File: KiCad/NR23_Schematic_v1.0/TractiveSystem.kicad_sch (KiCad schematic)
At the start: 3 parts

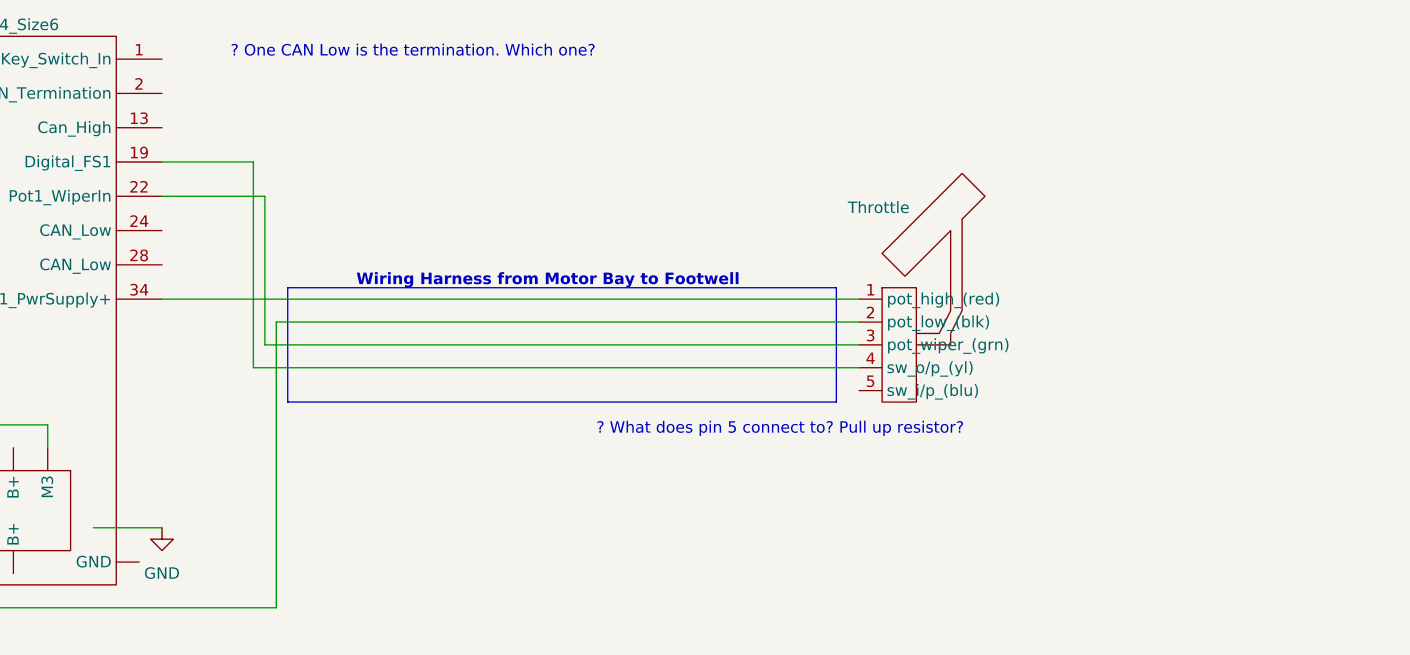
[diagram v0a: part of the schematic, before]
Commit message: added pullup resistor to the throttle
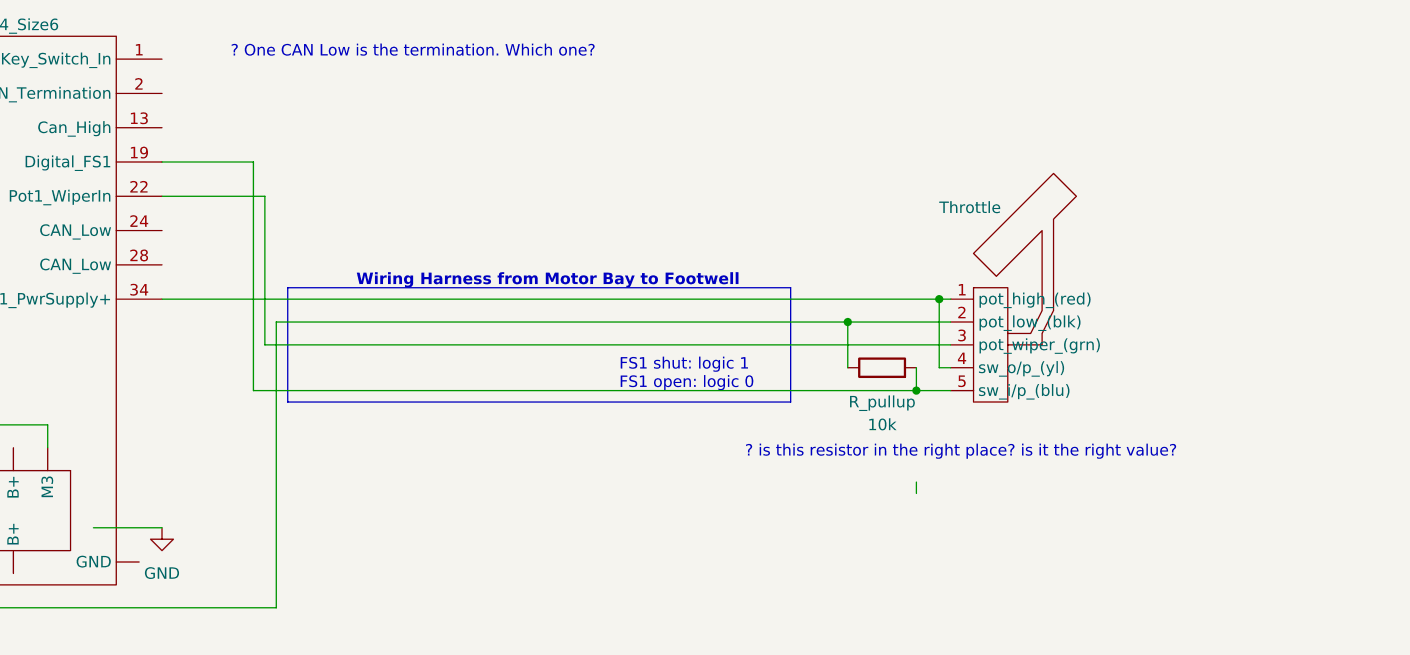
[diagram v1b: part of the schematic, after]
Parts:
- added R_pullup: 10k, symbol Device:R
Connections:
- net at U?.1 (pot_high_(red)), U?.34 (Pot1_PwrSupply+): now also U?.4 (sw_o/p_(yl))
- net at U?. (M3), U?.2 (pot_low_(blk)): now also R_pullup.1
- net at U?.19 (Digital_FS1): now also U?.5 (sw_i/p_(blu)), R_pullup.2; no longer U?.4 (sw_o/p_(yl))
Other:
- note added: "? is this resistor in the right place? is it the right value?"
- note added: "FS1 shut: logic 1 FS1 open: logic 0"
- note removed: "? What does pin 5 connect to? Pull up resistor?"
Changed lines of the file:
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@@
 (kicad_sch (version 20211123) (generator eeschema)
   (paper "A")
+  (junction (at 228.6 135.89) (diameter 0) (color 0 0 0 0)
+  )
+  (junction (at 231.14 125.73) (diameter 0) (color 0 0 0 0)
+  )
+  (junction (at 220.98 128.27) (diameter 0) (color 0 0 0 0)
+  )
   (bus_entry (at 88.9 180.34) (size 2.54 -2.54)
     (stroke (width 0) (type default) (color 0 0 0 0))
@@
     (stroke (width 0) (type default) (color 0 0 0 0))
   )
-  (polyline (pts (xy 219.71 124.46) (xy 158.75 124.46))
+  (polyline (pts (xy 214.63 124.46) (xy 158.75 124.46))
     (stroke (width 0) (type default) (color 0 0 0 0))
   )
@@
     (stroke (width 0) (type default) (color 0 0 0 0))
   )
+  (wire (pts (xy 154.94 110.49) (xy 154.94 135.89))
+    (stroke (width 0) (type default) (color 0 0 0 0))
+  )
   (polyline (pts (xy 106.68 135.89) (xy 45.72 135.89))
     (stroke (width 0) (type default) (color 0 0 0 0))
   )
+  (wire (pts (xy 154.94 135.89) (xy 228.6 135.89))
+    (stroke (width 0) (type default) (color 0 0 0 0))
+  )
   (polyline (pts (xy 55.88 170.18) (xy 55.88 146.05))
     (stroke (width 0) (type default) (color 0 0 0 0))
   )
+  (wire (pts (xy 220.98 128.27) (xy 232.41 128.27))
+    (stroke (width 0) (type default) (color 0 0 0 0))
+  )
   (wire (pts (xy 124.46 142.24) (xy 124.46 140.97))
     (stroke (width 0) (type default) (color 0 0 0 0))
   )
-  (wire (pts (xy 144.78 125.73) (xy 222.25 125.73))
+  (wire (pts (xy 144.78 125.73) (xy 231.14 125.73))
     (stroke (width 0) (type default) (color 0 0 0 0))
   )
@@
     (stroke (width 0) (type default) (color 0 0 0 0))
   )
+  (wire (pts (xy 228.6 135.89) (xy 232.41 135.89))
+    (stroke (width 0) (type default) (color 0 0 0 0))
+  )
+  (wire (pts (xy 220.98 128.27) (xy 220.98 133.35))
+    (stroke (width 0) (type default) (color 0 0 0 0))
+  )
   (wire (pts (xy 156.21 130.81) (xy 156.21 114.3))
     (stroke (width 0) (type default) (color 0 0 0 0))
@@
     (stroke (width 0) (type default) (color 0 0 0 0))
   )
-  (wire (pts (xy 157.48 128.27) (xy 222.25 128.27))
+  (wire (pts (xy 157.48 128.27) (xy 220.98 128.27))
     (stroke (width 0) (type default) (color 0 0 0 0))
   )
@@
     (stroke (width 0) (type default) (color 0 0 0 0))
   )
+  (wire (pts (xy 228.6 133.35) (xy 228.6 135.89))
+    (stroke (width 0) (type default) (color 0 0 0 0))
+  )
   (wire (pts (xy 50.8 175.26) (xy 55.88 175.26))
     (stroke (width 0) (type default) (color 0 0 0 0))
   )
-  (polyline (pts (xy 158.75 137.16) (xy 219.71 137.16))
+  (polyline (pts (xy 158.75 137.16) (xy 214.63 137.16))
     (stroke (width 0) (type default) (color 0 0 0 0))
   )
@@
     (stroke (width 0) (type default) (color 0 0 0 0))
   )
+  (wire (pts (xy 231.14 125.73) (xy 231.14 133.35))
+    (stroke (width 0) (type default) (color 0 0 0 0))
+  )
   (wire (pts (xy 85.09 176.53) (xy 88.9 176.53))
     (stroke (width 0) (type default) (color 0 0 0 0))
@@
     (stroke (width 0) (type default) (color 0 0 0 0))
   )
+  (wire (pts (xy 228.6 146.05) (xy 228.6 147.32))
+    (stroke (width 0) (type default) (color 0 0 0 0))
+  )
   (wire (pts (xy 85.09 172.72) (xy 88.9 172.72))
     (stroke (width 0) (type default) (color 0 0 0 0))
@@
     (stroke (width 0) (type default) (color 0 0 0 0))
   )
-  (wire (pts (xy 154.94 133.35) (xy 154.94 110.49))
-    (stroke (width 0) (type default) (color 0 0 0 0))
-  )
-  (wire (pts (xy 222.25 133.35) (xy 154.94 133.35))
+  (wire (pts (xy 232.41 133.35) (xy 231.14 133.35))
     (stroke (width 0) (type default) (color 0 0 0 0))
   )
@@
     (stroke (width 0) (type default) (color 0 0 0 0))
   )
-  (polyline (pts (xy 219.71 124.46) (xy 219.71 137.16))
+  (polyline (pts (xy 214.63 124.46) (xy 214.63 137.16))
     (stroke (width 0) (type default) (color 0 0 0 0))
   )
@@
     (stroke (width 0) (type default) (color 0 0 0 0))
   )
-  (wire (pts (xy 156.21 130.81) (xy 222.25 130.81))
+  (wire (pts (xy 156.21 130.81) (xy 232.41 130.81))
     (stroke (width 0) (type default) (color 0 0 0 0))
   )
@@
     (stroke (width 0) (type default) (color 0 0 0 0))
   )
+  (wire (pts (xy 231.14 125.73) (xy 232.41 125.73))
+    (stroke (width 0) (type default) (color 0 0 0 0))
+  )
   (wire (pts (xy 157.48 160.02) (xy 157.48 128.27))
     (stroke (width 0) (type default) (color 0 0 0 0))
@@
     (effects (font (size 1.27 1.27)) (justify left bottom))
   )
-  (text "? What does pin 5 connect to? Pull up resistor?" (at 193.04 140.97 0)
+  (text "? is this resistor in the right place? is it the right value?"
+    (at 209.55 143.51 0)
+    (effects (font (size 1.27 1.27)) (justify left bottom))
+  )
+  (text "FS1 shut: logic 1\nFS1 open: logic 0" (at 195.58 135.89 0)
     (effects (font (size 1.27 1.27)) (justify left bottom))
   )
@@
     (effects (font (size 1.27 1.27)) (justify left bottom))
   )
-  (symbol (lib_id "CamachosSymbols:Throttle") (at 232.41 127 0) (unit 1)
+  (symbol (lib_id "CamachosSymbols:Throttle") (at 242.57 127 0) (unit 1)
     (in_bom yes) (on_board yes)
-    (property "Reference" "U?" (id 0) (at 223.52 123.19 0)
-      (effects (font (size 1.27 1.27)) hide)
-    )
-    (property "Value" "Throttle" (id 1) (at 220.98 115.57 0)
+    (property "Reference" "U?" (id 0) (at 233.68 123.19 0)
+      (effects (font (size 1.27 1.27)) hide)
+    )
+    (property "Value" "Throttle" (id 1) (at 231.14 115.57 0)
       (effects (font (size 1.27 1.27)) (justify left))
     )
-    (property "Footprint" "" (id 2) (at 232.41 127 0)
-      (effects (font (size 1.27 1.27)) hide)
-    )
-    (property "Datasheet" "" (id 3) (at 232.41 127 0)
+    (property "Footprint" "" (id 2) (at 242.57 127 0)
+      (effects (font (size 1.27 1.27)) hide)
+    )
+    (property "Datasheet" "" (id 3) (at 242.57 127 0)
       (effects (font (size 1.27 1.27)) hide)
     )
@@
     (pin "34")
   )
+  (symbol (lib_id "Device:R") (at 224.79 133.35 90) (unit 1)
+    (in_bom yes) (on_board yes)
+    (property "Reference" "R_pullup" (id 0) (at 224.79 137.16 90))
+    (property "Value" "10k" (id 1) (at 224.79 139.7 90))
+    (property "Footprint" "" (id 2) (at 224.79 135.128 90)
+      (effects (font (size 1.27 1.27)) hide)
+    )
+    (property "Datasheet" "~" (id 3) (at 224.79 133.35 0)
+      (effects (font (size 1.27 1.27)) hide)
+    )
+    (pin "1")
+    (pin "2")
+  )
   (symbol (lib_id "power:GND") (at 144.78 151.13 0) (unit 1)

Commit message: end of class 07FEB23
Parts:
- added BT?: 7.2KW_Battery, symbol CamachosSymbols:7.2KW_Battery
- added F? (x2): Fuse, symbol Device:Fuse
- added K?: Line Contactor, Relay_THT:Relay_1P1T_NO_10x24x18.8mm_Panasonic_ADW11xxxxW_THT, symbol Relay:ADW11
- added SW?: Key Switch, symbol Switch:SW_SPST
- renumbered R_pullup to R_pulldown
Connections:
- net at U?. (M3): now also F?.2
- net at U?.1 (Key_Switch_In): now also SW?.2 (B)
- net M1: no longer names the net of M?.1, U?. (M3)
- net M2: no longer names the net of M?.2, U?. (M3)
- net M3: no longer names the net of M?.3, U?. (M3)
- new net: BT?.2 (-), U?. (M3)
- new net: F?.1, K?.4, U?. (M3)
- new net: K?.1, U?.3 (Line_Contactor_(Cont1))
- new net: K?.2, U?.4 (Cont1_Supply)
- new net: BT?.1 (+), F?.1
- new net: F?.2, K?.3
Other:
- note added: "? what are these fuses rated to?"
- note added: "? where does the other side of the key switch go?"
- note added: "FS1 Pedal pressed: logic 1 Pedal static: logic 0"
- note added: "Task: find pinout & wire these to the Sevcon"
- note added: "This throttle is not FSAE compliant in this design."
- note added: "Three large power wires to the motor"
- note added: "task: this battery schematic needs some updating"
- note removed: "? is this resistor in the right place? is it the right value?"
- note removed: "FS1 shut: logic 1 FS1 open: logic 0"
- note removed: "Three big wires from the motor"
- moved on the sheet: R_pulldown

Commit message: middle of class 08feb23
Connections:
- net at U?. (M3): now also F?.2
- net at F?.1: now also BT?.+; no longer BT?.1 (+)
- new net: BT?.-, U?. (M3)
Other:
- moved on the sheet: F?, K?, M?, R_pulldown, SW?

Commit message: microcontroller
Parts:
- renumbered R_pulldown to R_pullup
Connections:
- net at U?. (M3): now also F?.2
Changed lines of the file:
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@@
   (symbol (lib_id "Device:R") (at 217.17 125.73 90) (unit 1)
     (in_bom yes) (on_board yes)
-    (property "Reference" "R_pulldown" (id 0) (at 217.17 129.54 90))
+    (property "Reference" "R_pullup" (id 0) (at 217.17 129.54 90))
     (property "Value" "10k" (id 1) (at 217.17 132.08 90))
     (property "Footprint" "" (id 2) (at 217.17 127.508 90)

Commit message: microcontroller + symbol library
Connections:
- net at U?. (M3): now also F?.2

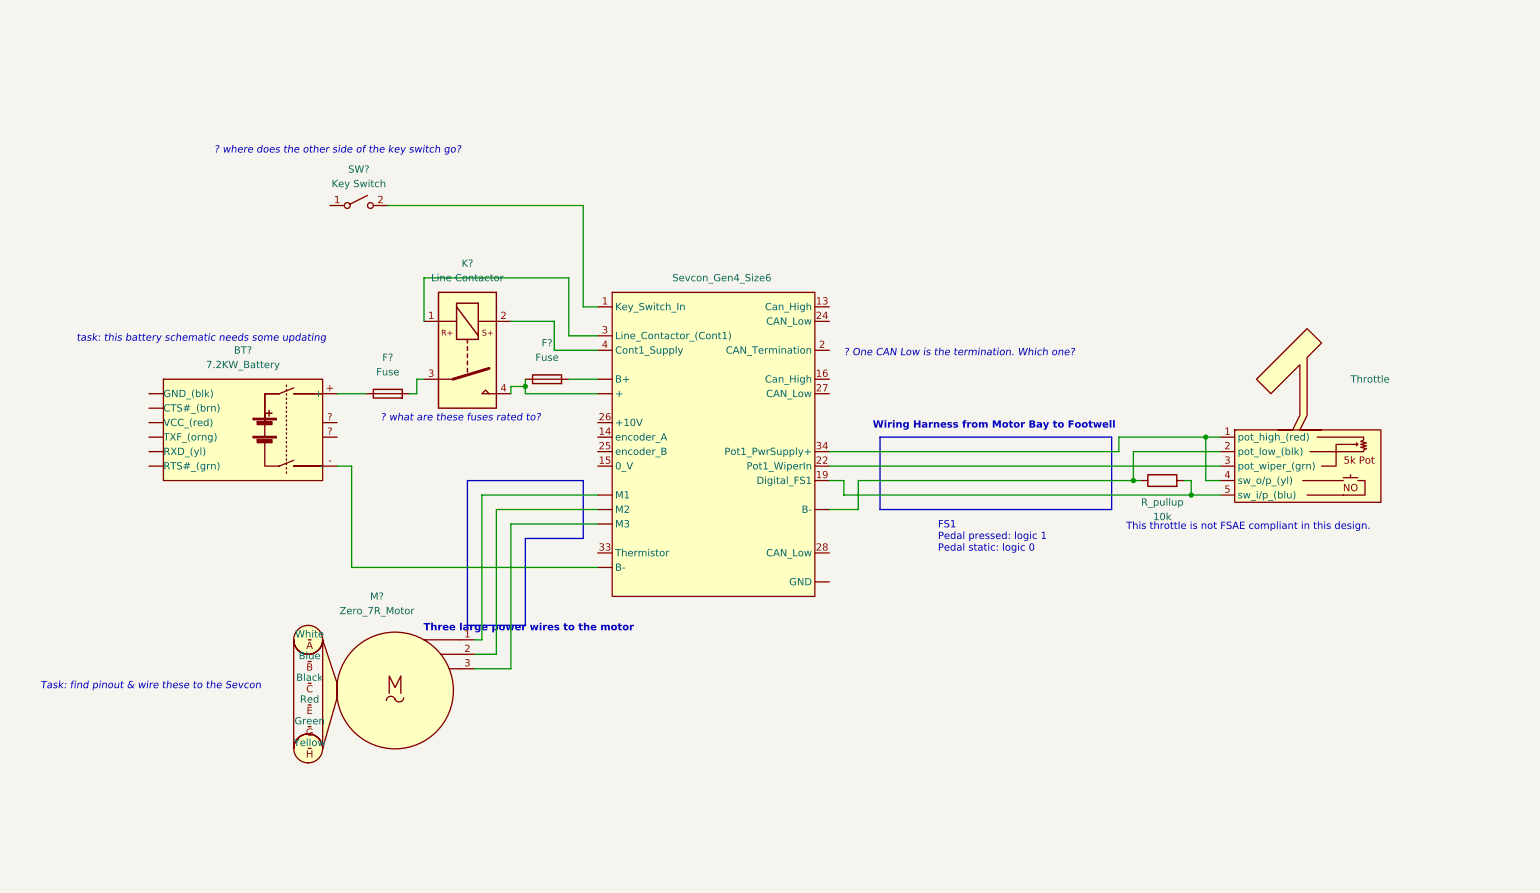
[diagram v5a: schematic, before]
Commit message: motor update
added the motor wiring to the tractive system
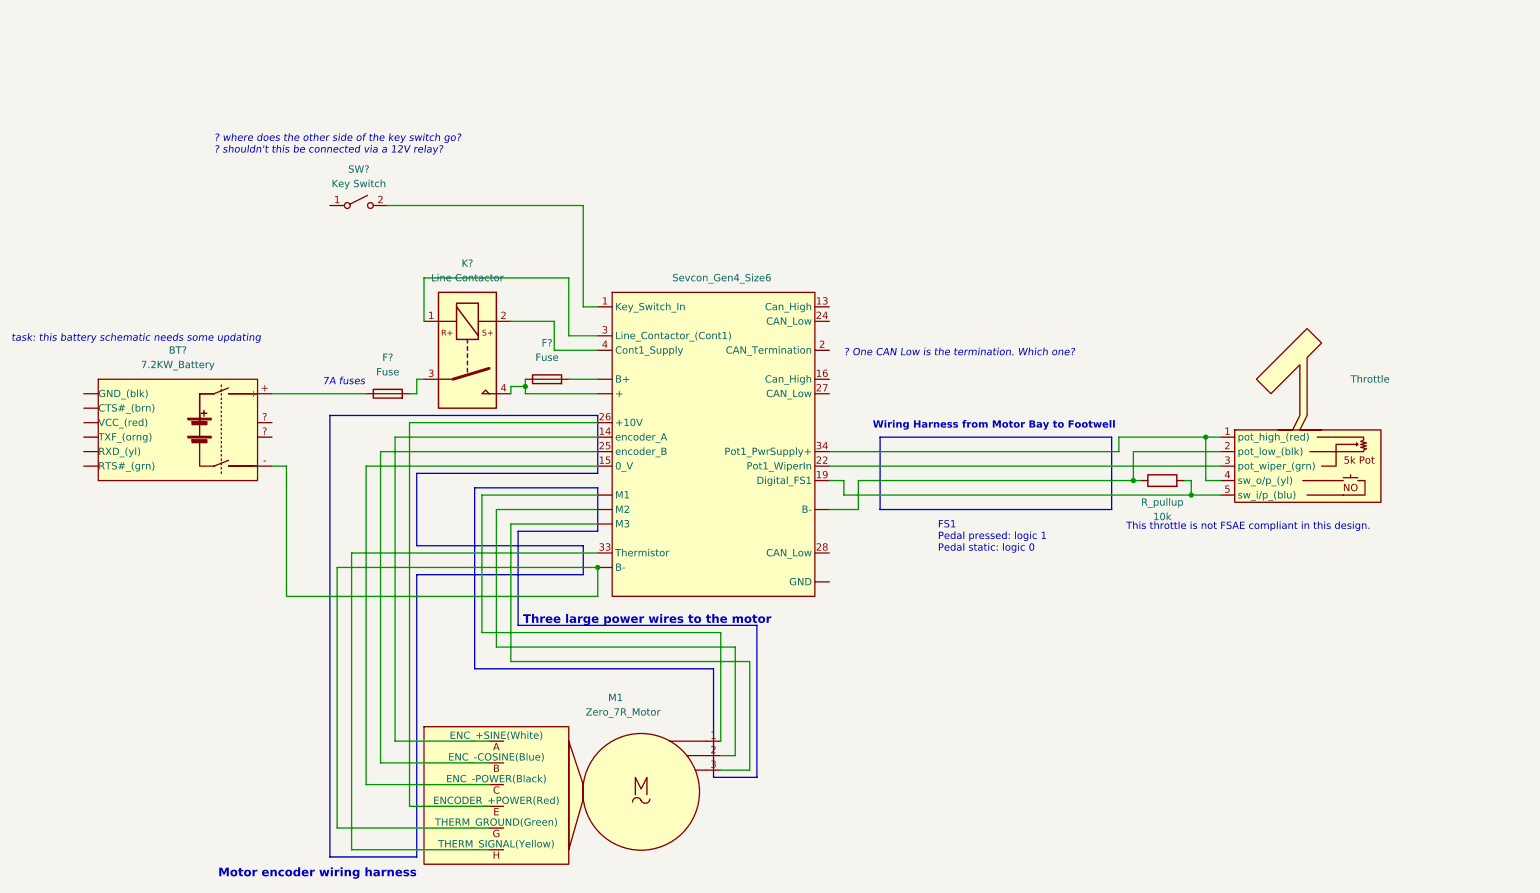
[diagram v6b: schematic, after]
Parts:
- gave numbers to parts that had none: 1
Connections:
- net at M1.A (ENC_+SINE(White)): now also U?.14 (encoder_A)
- net at M1.B (ENC_-COSINE(Blue)): now also U?.25 (encoder_B)
- net at M1.C (ENC_-POWER(Black)): now also U?.15 (0_V)
- net at M1.E (ENCODER_+POWER(Red)): now also U?.26 (+10V)
- net at M1.G (THERM_GROUND(Green)): now also BT?.-, U?. (M3)
- net at M1.H (THERM_SIGNAL(Yellow)): now also U?.33 (Thermistor)
- net at U?. (M3): now also F?.2
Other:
- note added: "7A fuses"
- note added: "? where does the other side of the key switch go? ? shouldn't this be connected via a 12V relay?"
- note added: "Motor encoder wiring harness"
- note removed: "? what are these fuses rated to?"
- note removed: "? where does the other side of the key switch go?"
- note removed: "Task: find pinout & wire these to the Sevcon"
- moved on the sheet: BT?

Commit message: 2/15
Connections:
- net at M1.A (ENC_+SINE(White)): now also U?.21 (encoder_A); no longer U?.14 (encoder_A)
- net at M1.B (ENC_-COSINE(Blue)): now also U?.35 (encoder_B); no longer U?.25 (encoder_B)
- net at U?. (M3): now also F?.2
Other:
- note added: "Harness 1: Sevcon to Footwell"
- note removed: "Wiring Harness from Motor Bay to Footwell"
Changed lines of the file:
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@@
     (effects (font (size 1.27 1.27)) (justify left bottom))
   )
-  (text "Wiring Harness from Motor Bay to Footwell" (at 166.37 116.84 0)
+  (text "Harness 1: Sevcon to Footwell" (at 166.37 116.84 0)
     (effects (font (size 1.27 1.27) (thickness 0.254) bold) (justify left bottom))
   )
@@
     (pin "1")
     (pin "13")
-    (pin "14")
+    (pin "21")
     (pin "15")
     (pin "16")
@@
     (pin "22")
     (pin "24")
-    (pin "25")
+    (pin "35")
     (pin "26")
     (pin "27")
